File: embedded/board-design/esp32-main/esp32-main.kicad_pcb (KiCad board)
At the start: 2 copper layers, 70.5 x 135.5 mm, 83 parts, among them J1 Conn_ARM_JTAG_SWD_10, J2 Conn_01x08_Socket, J3 Conn_01x08_Socket, J4 0473460001, J5 Conn_01x02_Socket, J6 Conn_01x02_Socket, J7 Conn_01x03_Socket, Q1 BC817, Q2 BC817, Q3 FDN340P, Q4 FMMT720TA, Q5 FDN340P, Q6 FDN340P, U1 ESP32-WROVER-E, U2 BD48ExxG, U3 FT231XS, U4 TPS61090, U5 LTC4054ES5-4.2

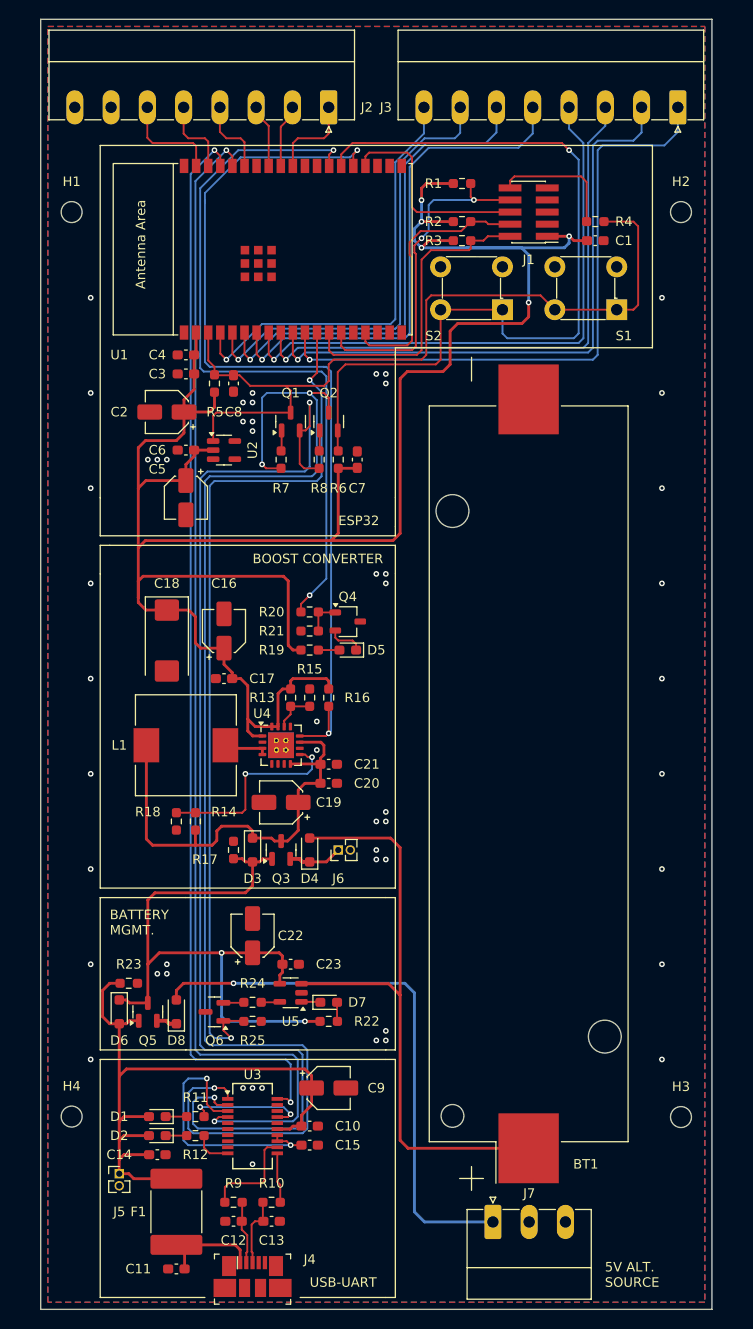
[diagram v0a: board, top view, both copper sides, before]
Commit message: [bike-embedded-app]
Added output for 3V3. Increased mounting holes.

Signed-off-by: Nicolae-Andrei Vasile <vasilenicolaeandrei@gmail.com>
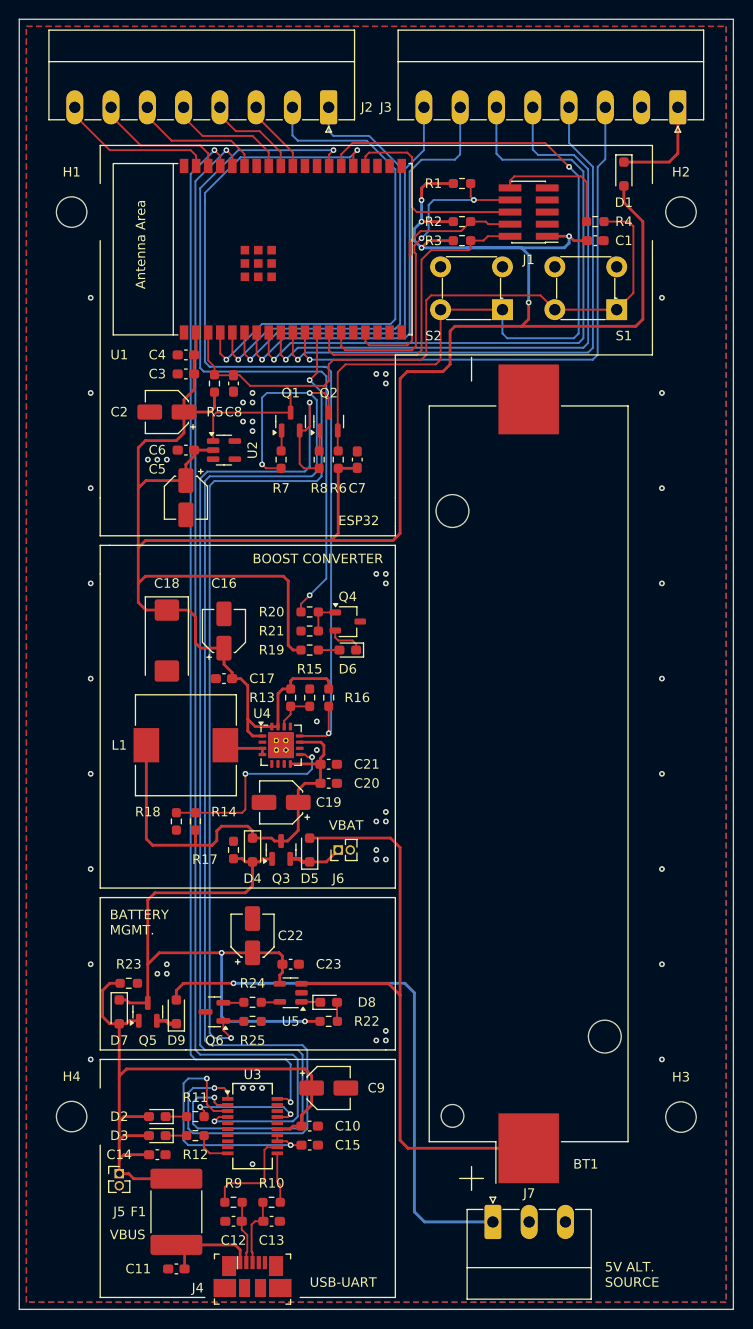
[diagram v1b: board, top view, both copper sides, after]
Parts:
- added D9: SMD22WS-TP, Diode_SMD:D_SOD-323_HandSoldering, F.Cu at (124.0, 125.0)
- D1: value LED(GREEN) -> SMD22WS-TP; footprint LED_SMD:LED_0603_1608Metric_Pad1.05x0.95mm_HandSolder -> Diode_SMD:D_SOD-323_HandSoldering
- D2: value LED(RED) -> LED(GREEN)
- D3, D6, D8: value SMD22WS-TP -> LED(RED); footprint Diode_SMD:D_SOD-323_HandSoldering -> LED_SMD:LED_0603_1608Metric_Pad1.05x0.95mm_HandSolder
- D5, D7: value LED(RED) -> SMD22WS-TP; footprint LED_SMD:LED_0603_1608Metric_Pad1.05x0.95mm_HandSolder -> Diode_SMD:D_SOD-323_HandSoldering
- H1, H2, H3, H4: footprint MountingHole:MountingHole_2.2mm_M2 -> MountingHole:MountingHole_3.2mm_M3
- moved D1 110.5 mm to (171.0, 37.0), turned to -90 degrees
- moved D6 44.9 mm to (142.0, 87.0), turned to 180 degrees
- moved D3 31.6 mm to (122.0, 138.0), turned to 180 degrees
- moved D7 22.0 mm to (118.0, 125.0), turned to -90 degrees
- moved D5 21.4 mm to (138.0, 108.0), turned to 90 degrees
- moved D8 16.0 mm to (140.0, 124.0), turned to 0 degrees
- moved D4 6.00 mm to (132.0, 108.0), turned to -90 degrees
- moved D2 2.00 mm to (122.0, 136.0)
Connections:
- C19 pad 1: Net-(D3-K) -> Net-(D4-K)
- C20 pad 1: Net-(D3-K) -> Net-(D4-K)
- C21 pad 1: Net-(D3-K) -> Net-(D4-K)
- D1 pad 2: VBUS -> +3V3
- D3 pad 2: +5V -> VBUS
- D4 pad 1: /power-supply/VBAT_TEST -> Net-(D4-K)
- D4 pad 2: VBAT -> +5V
- D5 pad 1: Net-(D5-K) -> /power-supply/VBAT_TEST
- D5 pad 2: Net-(D5-A) -> VBAT
- D6 pad 1: +5V -> Net-(D6-K)
- D6 pad 2: VBUS -> Net-(D6-A)
- D7 pad 1: Net-(D7-K) -> +5V
- D7 pad 2: Net-(D7-A) -> VBUS
- D8 pad 2: /battery/ALT -> Net-(D8-A)
- J2 pad 1: /GPIO5/VSPICS0 -> /GPIO39
- J2 pad 2: /GPIO18/VSPICLK -> /GPIO36
- J2 pad 3: /GPIO19/VSPIQ -> /GPIO5/VSPICS0
- J2 pad 4: /GPIO21/VSPIHD -> /GPIO18/VSPICLK
- J2 pad 5: /GPIO22/VSPIWP -> /GPIO19/VSPIQ
- J2 pad 6: /GPIO23/VSPID -> /GPIO21/VSPIHD
- J2 pad 7: unconnected-(J2-Pin_7-Pad7) -> /GPIO22/VSPIWP
- J2 pad 8: unconnected-(J2-Pin_8-Pad8) -> /GPIO23/VSPID
- J3 pad 1: /GPIO26 -> Net-(D1-K)
- J3 pad 2: /GPIO25 -> GND
- J3 pad 3: /GPIO33 -> /GPIO26
- J3 pad 4: /GPIO32 -> /GPIO25
- J3 pad 5: /GPIO35 -> /GPIO33
- J3 pad 6: /GPIO34 -> /GPIO32
- J3 pad 7: /GPIO39 -> /GPIO35
- J3 pad 8: /GPIO36 -> /GPIO34
- L1 pad 1: Net-(D3-K) -> Net-(D4-K)
- Q3 pad 3: Net-(D3-K) -> Net-(D4-K)
- Q4 pad 2: Net-(D5-K) -> Net-(D6-K)
- Q5 pad 2: Net-(D8-K) -> Net-(D9-K)
- R11 pad 2: Net-(D1-K) -> Net-(D2-K)
- R12 pad 2: Net-(D2-K) -> Net-(D3-K)
- R14 pad 1: Net-(D3-K) -> Net-(D4-K)
- R19 pad 2: Net-(D5-A) -> Net-(D6-A)
- R22 pad 2: Net-(D7-A) -> Net-(D8-A)
- U4 pad 11: Net-(D3-K) -> Net-(D4-K)
- U4 pad 8: Net-(D3-K) -> Net-(D4-K)
- U5 pad 1: Net-(D7-K) -> Net-(D8-K)
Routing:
- net Net-(D4-K): track 0.00 -> 47.5 mm
- net Net-(D3-K): track 47.5 -> 2.21 mm
- net +3V3: track 237.9 -> 264.3 mm
- net Net-(D1-K): track 2.21 -> 10.9 mm
- net /GPIO36: track 46.1 -> 54.4 mm
- net /GPIO32: track 61.4 -> 68.8 mm
- net /GPIO26: track 66.8 -> 59.8 mm
- net /GPIO34: track 51.6 -> 44.8 mm
- net /GPIO35: track 54.4 -> 47.7 mm
- net /GPIO19/VSPIQ: track 6.69 -> 12.9 mm
- net /GPIO21/VSPIHD: track 8.10 -> 14.0 mm
- net /GPIO22/VSPIWP: track 8.25 -> 14.0 mm
- net /GPIO23/VSPID: track 10.8 -> 16.4 mm
- net /GPIO33: track 61.0 -> 64.9 mm
- net Net-(D6-K): track 0.00 -> 3.83 mm
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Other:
- board size 70.5 x 135.5 mm -> 75 x 135.5 mm
- board text added: "VBAT"
- board text added: "VBUS"
